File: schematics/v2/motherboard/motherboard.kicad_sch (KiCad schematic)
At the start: 23 parts, among them J1 RJ45_Abracon_ARJP11A-MASA-B-A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, J2 12V Alt Supply, J3 S1, J4 S2, J5 SDI1, J6 SDI2, U1 Controller_Module, U2 Signal_Module, U3 Power_Module

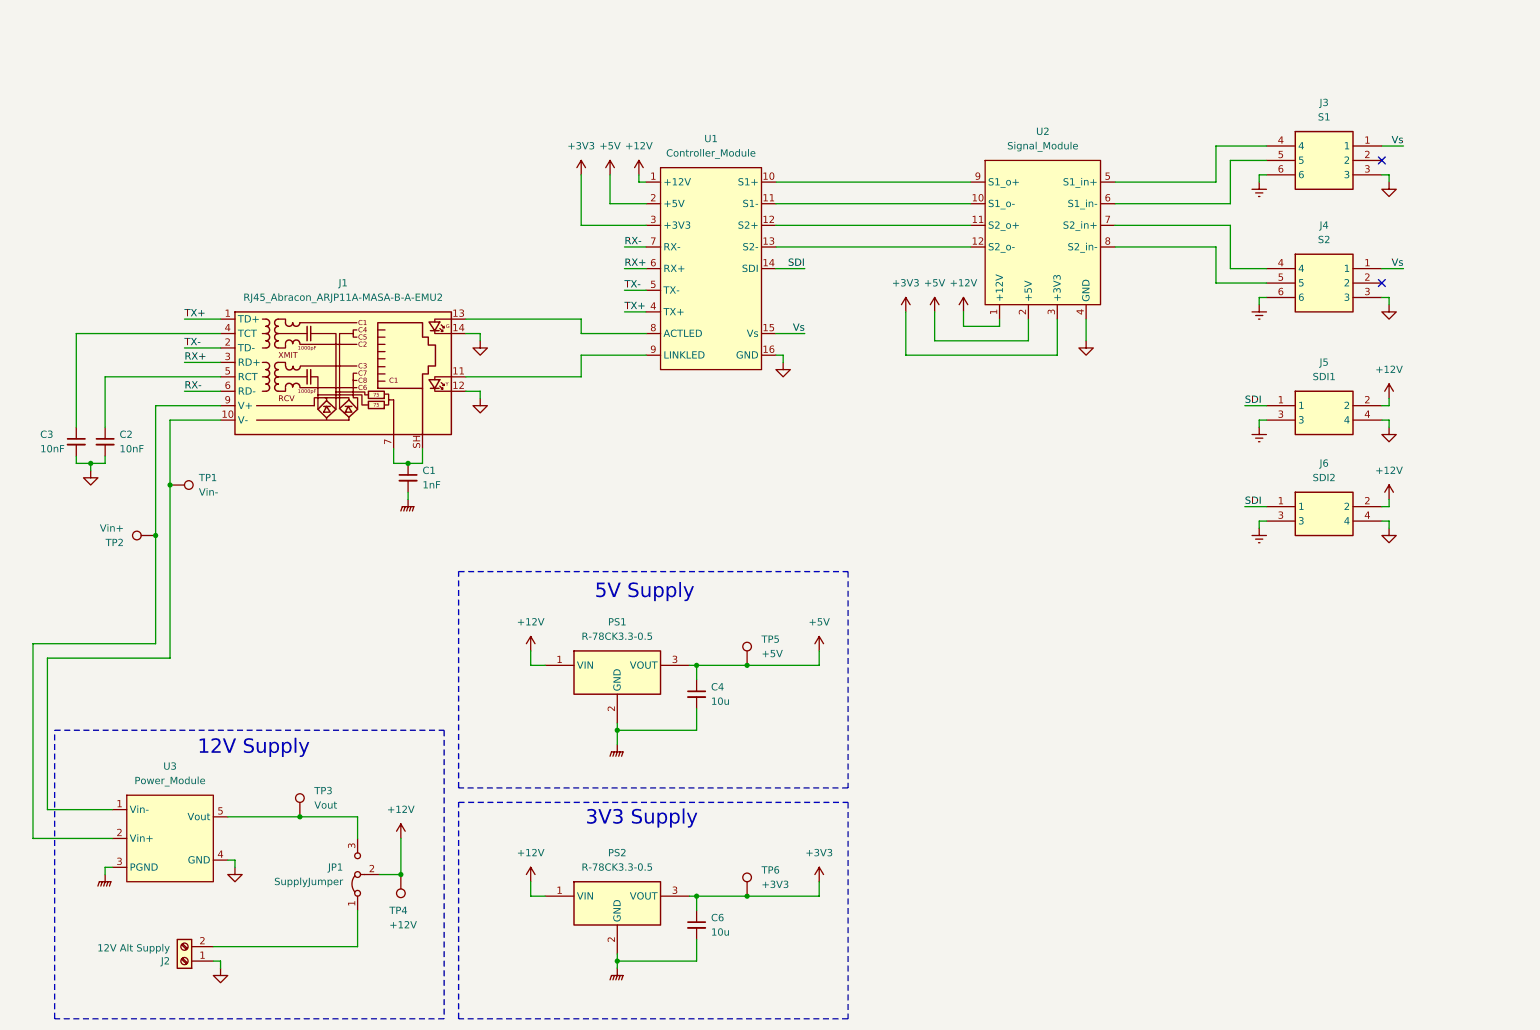
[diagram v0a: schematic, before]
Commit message: link controller module: version 1
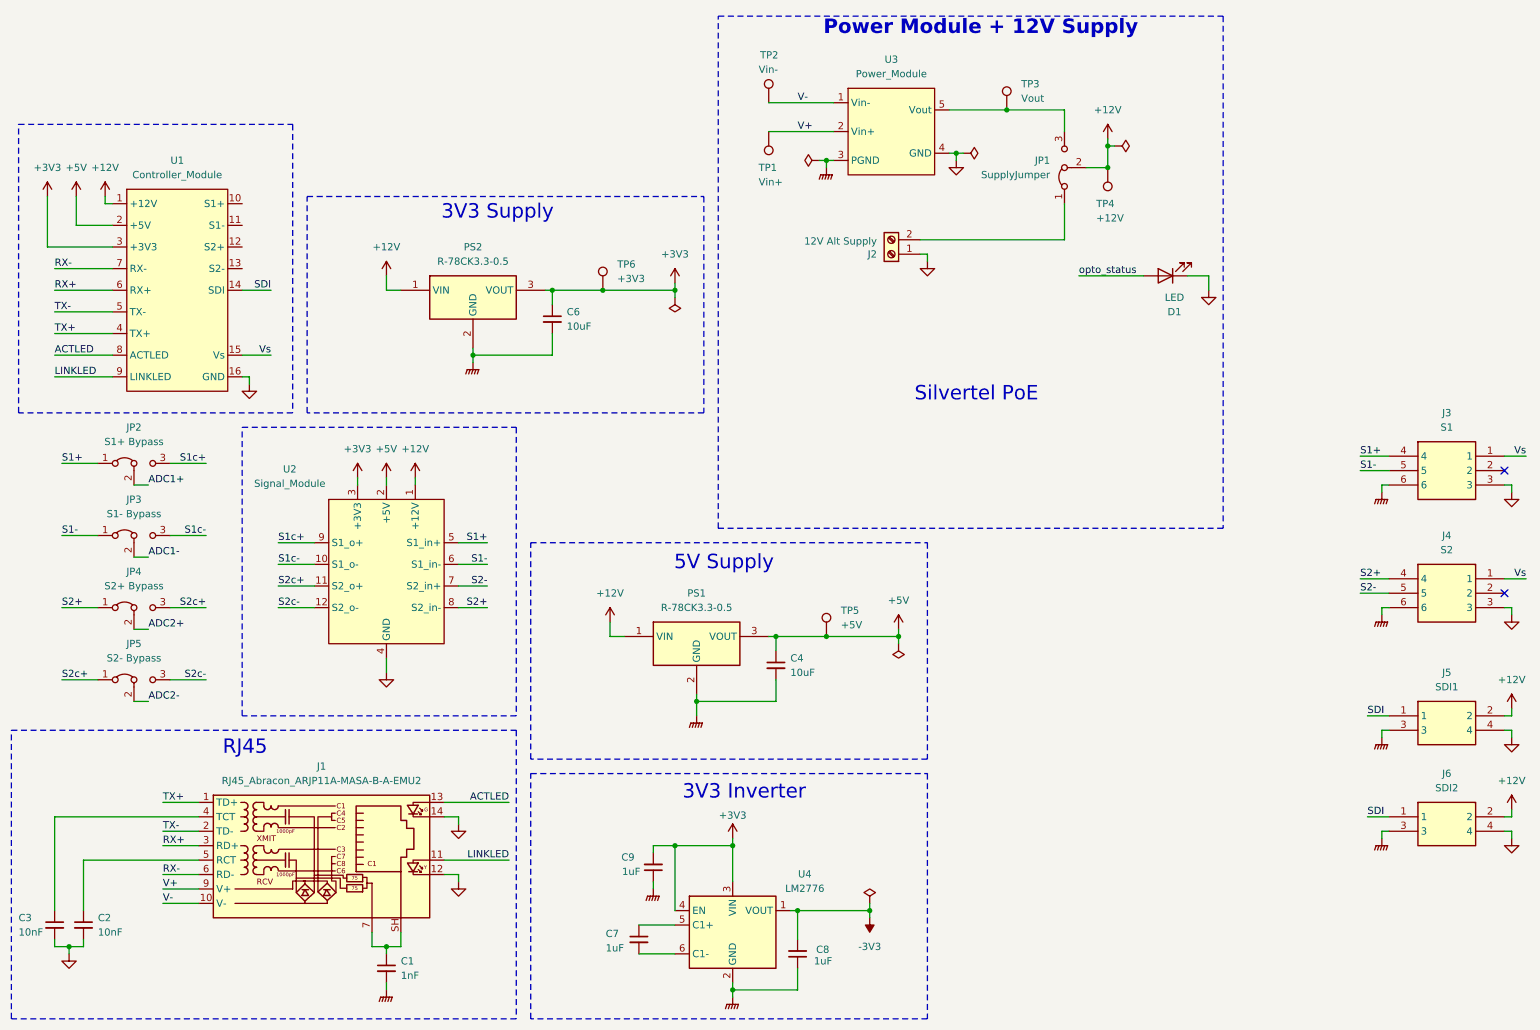
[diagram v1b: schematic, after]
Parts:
- added C7, C8, C9: 1uF, symbol Device:C_Small
- added D1: LED, symbol Device:LED
- added JP2: S1+ Bypass, symbol Jumper:Jumper_3_Bridged12
- added JP3: S1- Bypass, symbol Jumper:Jumper_3_Bridged12
- added JP4: S2+ Bypass, symbol Jumper:Jumper_3_Bridged12
- added JP5: S2- Bypass, symbol Jumper:Jumper_3_Bridged12
- added U4: LM2776, Package_TO_SOT_SMD:SOT-23-6, symbol Regulator_SwitchedCapacitor:LM2776
- C4, C6: value 10u -> 10uF
- TP1: value Vin- -> Vin+
- TP2: value Vin+ -> Vin-
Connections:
- net Earth is gone; now on net GNDPWR: J3.6, J4.6, J5.3, J6.3
- net +3V3: now also C9.2, U4.3 (VIN), U4.4 (EN)
- net GND: now also D1.1 (K)
- net GNDPWR: now also C8.1, C9.1, U4.2 (GND)
- net V-: now reaches J1.10 (V-), U3.1 (Vin-)
- net V-: now also TP2.1; no longer TP1.1
- net V+: now reaches J1.9 (V+), U3.2 (Vin+)
- net V+: now also TP1.1; no longer TP2.1
- net S2+: now reaches J4.4
- net S2+: now also U2.8 (S2_in-), JP4.1 (A); no longer U2.7 (S2_in+)
- net S2-: now reaches J4.5
- net S2-: now also U2.7 (S2_in+); no longer U2.8 (S2_in-)
- net LINKLED: now reaches J1.11, U1.9 (LINKLED)
- net ACTLED: now reaches J1.13, U1.8 (ACTLED)
- net at U1.11 (S1-): no longer U2.10 (S1_o-)
- net at U1.12 (S2+): no longer U2.11 (S2_o+)
- net at U1.13 (S2-): no longer U2.12 (S2_o-)
- net S1+: now reaches J3.4, U2.5 (S1_in+)
- net S1+: now also JP2.1 (A)
- net S1-: now reaches J3.5, U2.6 (S1_in-)
- net S1-: now also JP3.1 (A)
- net at U1.10 (S1+): no longer U2.9 (S1_o+)
- new net: C7.1, U4.5 (C1+)
- new net: C7.2, U4.6 (C1-)
- new net -3V3: C8.2, U4.1 (VOUT)
- new net ADC1+: JP2.2 (C)
- new net ADC1-: JP3.2 (C)
- new net ADC2+: JP4.2 (C)
- new net ADC2-: JP5.2 (C)
- new net S1c+: JP2.3 (B), U2.9 (S1_o+)
- new net S1c-: JP3.3 (B), U2.10 (S1_o-)
- new net S2c+: JP4.3 (B), JP5.1 (A), U2.11 (S2_o+)
- new net S2c-: JP5.3 (B), U2.12 (S2_o-)
- new net opto_status: D1.2 (A)
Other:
- note added: "3V3 Inverter"
- note added: "Power Module + 12V Supply"
- note added: "RJ45"
- note added: "Silvertel PoE"
- note removed: "12V Supply"
- moved on the sheet: C1, C2, C3, C4, C6, J1, J2, J3, J4, J5, J6, JP1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
